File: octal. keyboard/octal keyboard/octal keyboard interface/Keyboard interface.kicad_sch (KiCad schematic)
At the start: 75 parts, among them J1 Conn_01x16_Male, J2 Conn_01x06_Male, J3 Conn_01x01_Male, U1 DM9602, U2 74LS132, U3 74LS02, U4 74LS37, U5 7496, U6 74LS05

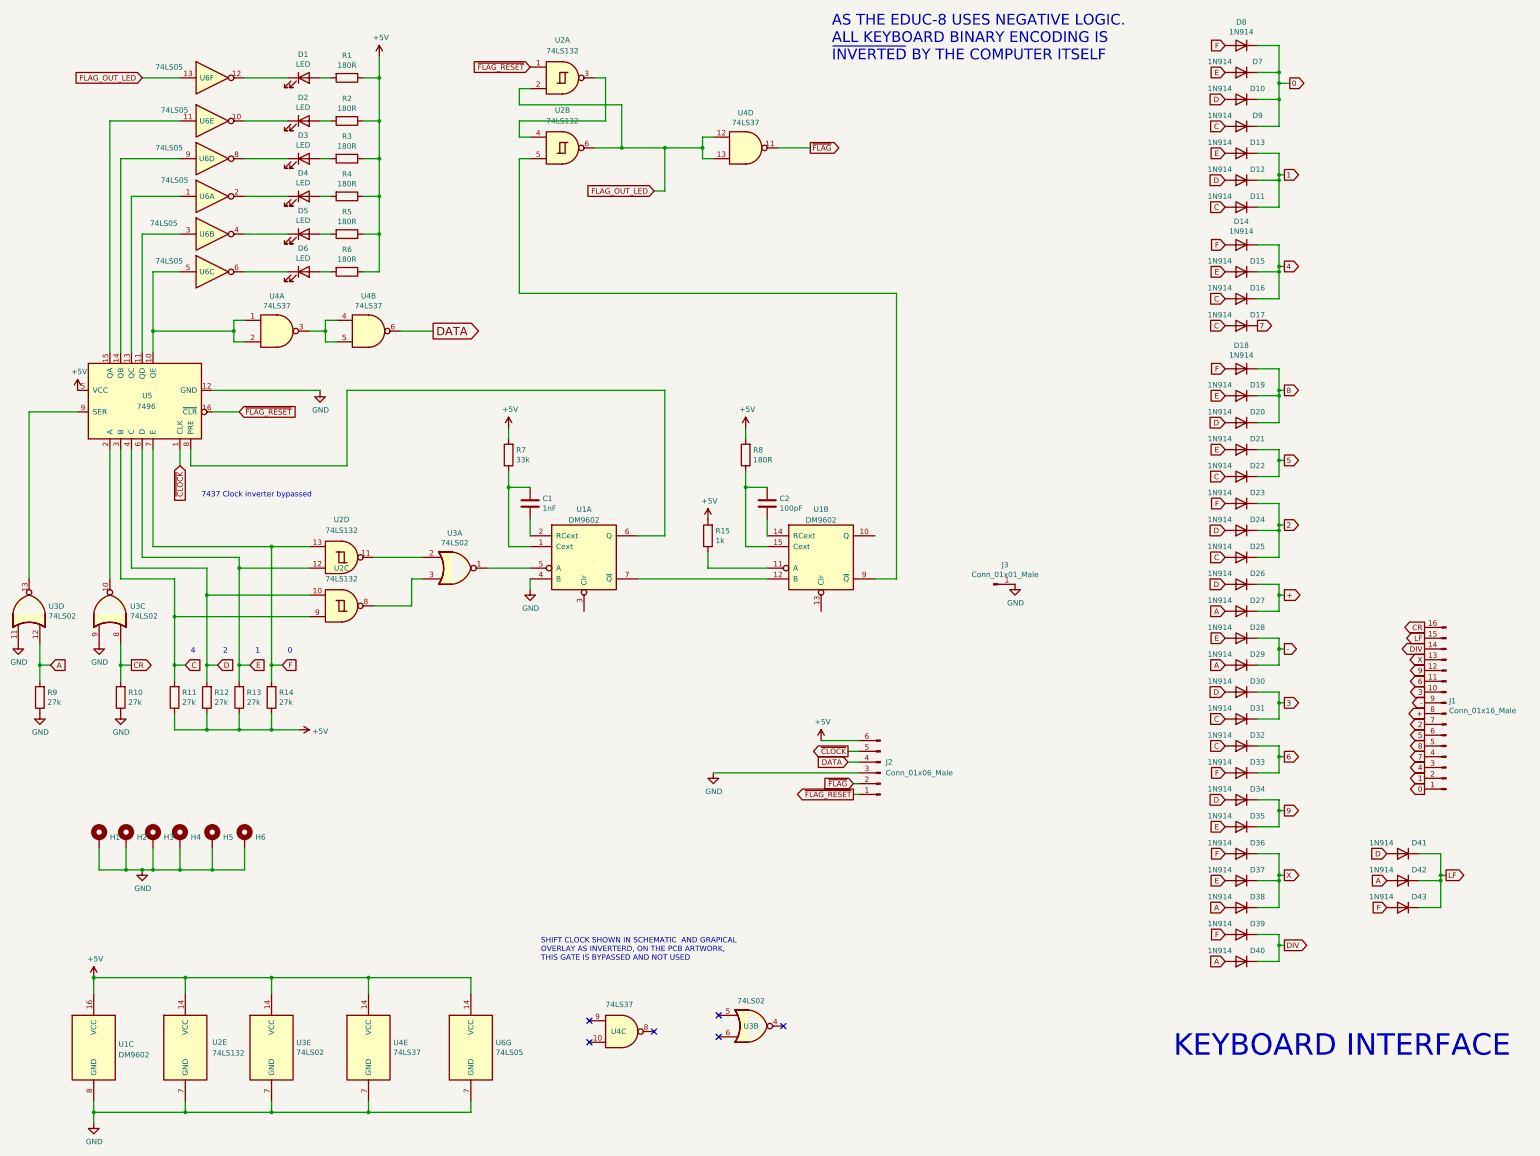
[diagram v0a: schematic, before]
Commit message: Changes 20-7-2025 E8/T. Connected 3 missing supply rail tracks to ICS Added flood fill top and bottom to reduce noise E8/F Corrected labelling on RHS board to reflect EXT_LA not GND Changed fast slow switch operation so fast is in the DOWN position. E8/C. Ran a new track to the 2 pin JST connector from EXT_LA from 10 pin connector on SR input. Added files for E8MX, 2k byte memory expansion board
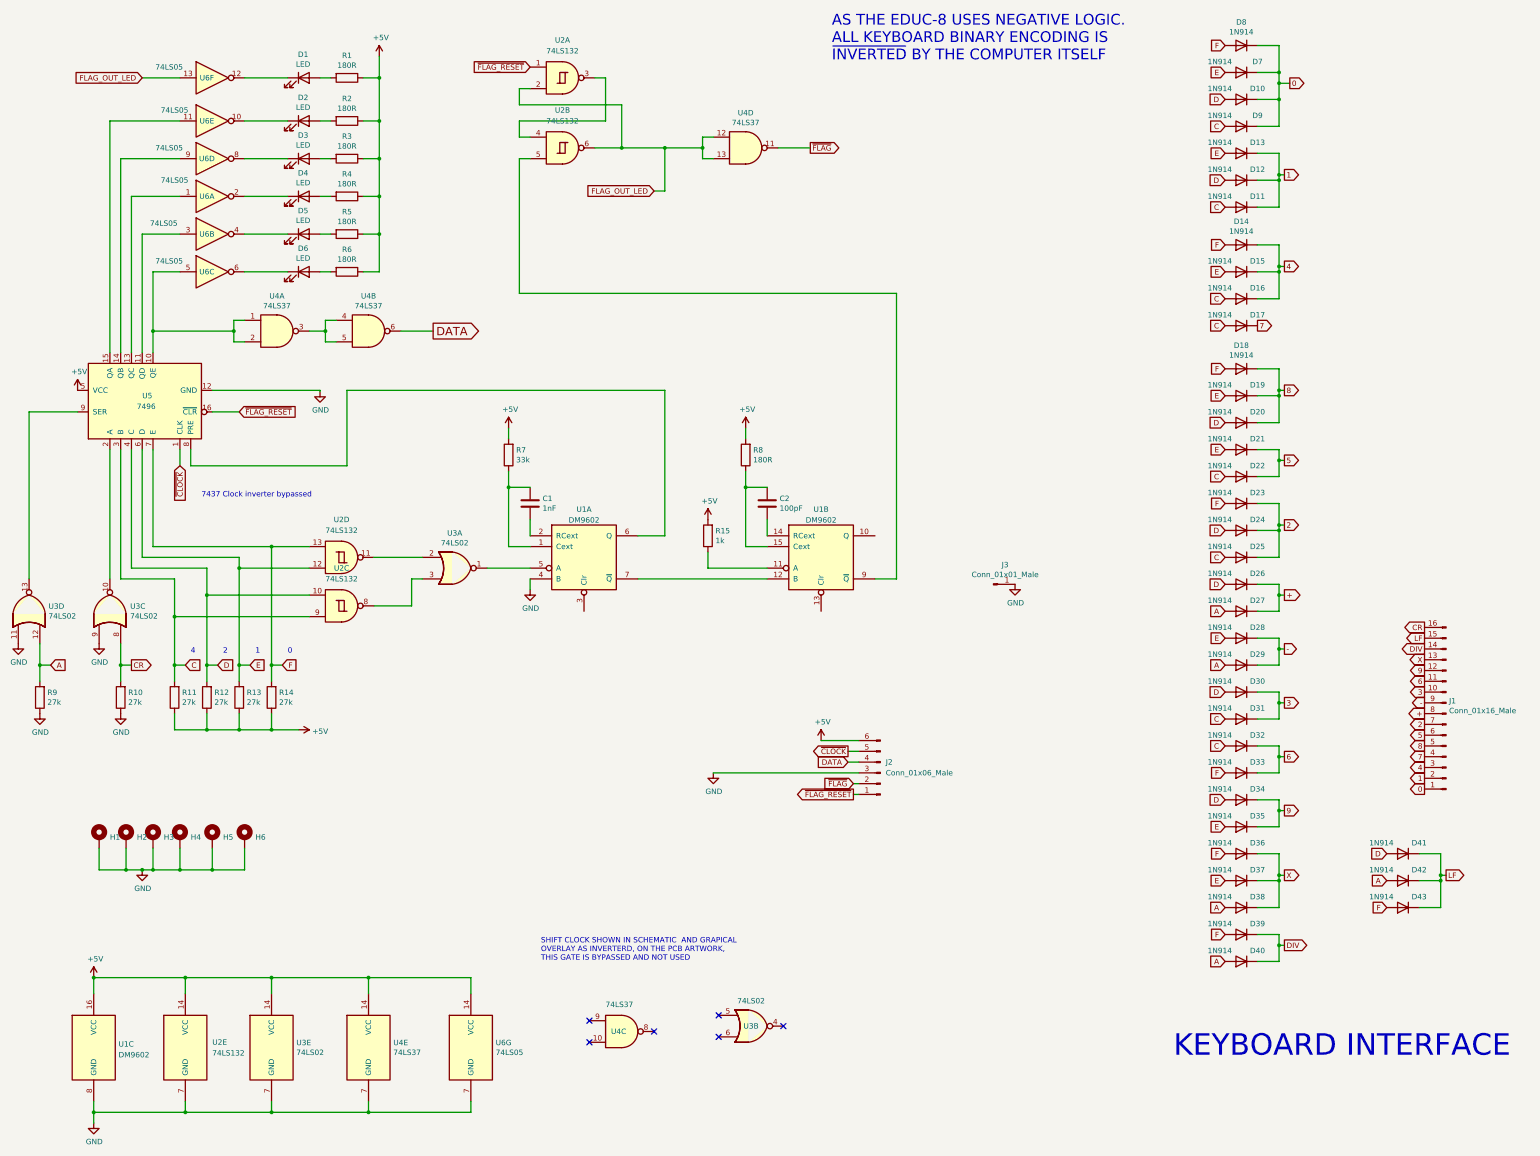
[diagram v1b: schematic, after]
